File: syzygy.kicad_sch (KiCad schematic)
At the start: 5 parts, among them J3 SYZYGY_STD, U11 SN74LVC2T45YZP, U13 ADC101C021CIMK

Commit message: Incremental Progress
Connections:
- net 3V3: no longer J3.40 (+3.3V)
- net VIO: no longer J3.39 (VIO)
- net 5V renamed SYZYGY_5V
- new net SYZYGY_3V3: J3.40 (+3.3V)
- new net SYZYGY_VIO: J3.39 (VIO)
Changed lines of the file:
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@@
+	)
+	(junction
+		(at 158.75 36.83)
+		(diameter 0)
+		(color 0 0 0 0)
 	)
 	(junction
@@
 		(color 0 0 0 0)
 	)
+	(junction
+		(at 158.75 87.63)
+		(diameter 0)
+		(color 0 0 0 0)
+	)
 	(no_connect
 		(at 130.81 67.31)
@@
 	(wire
 		(pts
-			(xy 120.65 87.63) (xy 130.81 87.63)
-		)
-		(stroke
-			(width 0)
-			(type default)
-		)
-	)
-	(wire
-		(pts
 			(xy 120.65 44.45) (xy 130.81 44.45)
 		)
@@
 	(wire
 		(pts
+			(xy 158.75 87.63) (xy 158.75 92.71)
+		)
+		(stroke
+			(width 0)
+			(type default)
+		)
+	)
+	(wire
+		(pts
+			(xy 158.75 36.83) (xy 161.29 36.83)
+		)
+		(stroke
+			(width 0)
+			(type default)
+		)
+	)
+	(wire
+		(pts
 			(xy 73.66 44.45) (xy 81.28 44.45)
 		)
@@
 	(wire
 		(pts
+			(xy 128.27 87.63) (xy 130.81 87.63)
+		)
+		(stroke
+			(width 0)
+			(type default)
+		)
+	)
+	(wire
+		(pts
 			(xy 45.72 105.41) (xy 46.99 105.41)
 		)
@@
 	(wire
 		(pts
+			(xy 158.75 34.29) (xy 158.75 36.83)
+		)
+		(stroke
+			(width 0)
+			(type default)
+		)
+	)
+	(wire
+		(pts
 			(xy 158.75 41.91) (xy 168.91 41.91)
 		)
@@
 	(wire
 		(pts
+			(xy 161.29 87.63) (xy 158.75 87.63)
+		)
+		(stroke
+			(width 0)
+			(type default)
+		)
+	)
+	(wire
+		(pts
 			(xy 45.72 105.41) (xy 45.72 110.49)
 		)
@@
 	(wire
 		(pts
+			(xy 158.75 36.83) (xy 158.75 39.37)
+		)
+		(stroke
+			(width 0)
+			(type default)
+		)
+	)
+	(wire
+		(pts
 			(xy 50.8 54.61) (xy 50.8 59.69)
 		)
@@
 	(wire
 		(pts
-			(xy 158.75 87.63) (xy 168.91 87.63)
-		)
-		(stroke
-			(width 0)
-			(type default)
-		)
-	)
-	(wire
-		(pts
 			(xy 35.56 49.53) (xy 50.8 49.53)
 		)
@@
 		(pts
 			(xy 118.11 77.47) (xy 118.11 80.01)
-		)
-		(stroke
-			(width 0)
-			(type default)
-		)
-	)
-	(wire
-		(pts
-			(xy 158.75 39.37) (xy 168.91 39.37)
 		)
 		(stroke
@@
 		)
 	)
-	(label "VIO"
-		(at 120.65 87.63 0)
-		(fields_autoplaced yes)
-		(effects
-			(font
-				(size 1.27 1.27)
-			)
-			(justify left bottom)
-		)
-	)
 	(label "3V3"
 		(at 81.28 39.37 270)
@@
 		)
 	)
-	(label "3V3"
-		(at 168.91 87.63 180)
-		(fields_autoplaced yes)
-		(effects
-			(font
-				(size 1.27 1.27)
-			)
-			(justify right bottom)
-		)
-	)
 	(label "I2C_ADC.SCL"
 		(at 35.56 52.07 0)
@@
 			)
 			(justify left bottom)
+		)
+	)
+	(global_label "SYZYGY_5V"
+		(shape passive)
+		(at 161.29 36.83 0)
+		(fields_autoplaced yes)
+		(effects
+			(font
+				(size 1.27 1.27)
+			)
+			(justify left)
+		)
+		(property "Intersheetrefs" "${INTERSHEET_REFS}"
+			(at 173.3844 36.83 0)
+			(effects
+				(font
+					(size 1.27 1.27)
+				)
+				(justify left)
+				(hide yes)
+			)
+		)
+	)
+	(global_label "SYZYGY_VIO"
+		(shape passive)
+		(at 128.27 87.63 180)
+		(fields_autoplaced yes)
+		(effects
+			(font
+				(size 1.27 1.27)
+			)
+			(justify right)
+		)
+		(property "Intersheetrefs" "${INTERSHEET_REFS}"
+			(at 115.4498 87.63 0)
+			(effects
+				(font
+					(size 1.27 1.27)
+				)
+				(justify right)
+				(hide yes)
+			)
+		)
+	)
+	(global_label "SYZYGY_3V3"
+		(shape passive)
+		(at 161.29 87.63 0)
+		(fields_autoplaced yes)
+		(effects
+			(font
+				(size 1.27 1.27)
+			)
+			(justify left)
+		)
+		(property "Intersheetrefs" "${INTERSHEET_REFS}"
+			(at 174.5939 87.63 0)
+			(effects
+				(font
+					(size 1.27 1.27)
+				)
+				(justify left)
+				(hide yes)
+			)
 		)
 	)
@@
 		)
 	)
-	(hierarchical_label "5V"
-		(shape passive)
-		(at 168.91 39.37 0)
-		(fields_autoplaced yes)
-		(effects
-			(font
-				(size 1.27 1.27)
-			)
-			(justify left)
-		)
-	)
 	(hierarchical_label "TDM{FS,DATA}"
 		(shape output)
@@
 		)
 	)
-	(hierarchical_label "VIO"
-		(shape passive)
-		(at 120.65 87.63 180)
-		(fields_autoplaced yes)
-		(effects
-			(font
-				(size 1.27 1.27)
-			)
-			(justify right)
-		)
-	)
 	(hierarchical_label "I2C_C{SCL,SDA}"
 		(shape bidirectional)
@@
 			)
 			(justify left)
+		)
+	)
+	(symbol
+		(lib_id "power:PWR_FLAG")
+		(at 158.75 34.29 0)
+		(unit 1)
+		(exclude_from_sim no)
+		(in_bom yes)
+		(on_board yes)
+		(dnp no)
+		(fields_autoplaced yes)
+		(property "Reference" "#FLG03"
+			(at 158.75 32.385 0)
+			(effects
+				(font
+					(size 1.27 1.27)
+				)
+				(hide yes)
+			)
+		)
+		(property "Value" "PWR_FLAG"
+			(at 158.75 29.21 0)
+			(effects
+				(font
+					(size 1.27 1.27)
+				)
+			)
+		)
+		(property "Footprint" ""
+			(at 158.75 34.29 0)
+			(effects
+				(font
+					(size 1.27 1.27)
+				)
+				(hide yes)
+			)
+		)
+		(property "Datasheet" "~"
+			(at 158.75 34.29 0)
+			(effects
+				(font
+					(size 1.27 1.27)
+				)
+				(hide yes)
+			)
+		)
+		(property "Description" "Special symbol for telling ERC where power comes from"
+			(at 158.75 34.29 0)
+			(effects
+				(font
+					(size 1.27 1.27)
+				)
+				(hide yes)
+			)
+		)
+		(pin "1"
+		)
+		(instances
+			(project "albert"
+				(path "/b16dfd04-6bfc-4d2d-ba2c-9a843d57dfb1/c7bb0f6a-a070-4074-9132-0f05f79fd133"
+					(reference "#FLG03")
+					(unit 1)
+				)
+			)
 		)
 	)
@@
 					(unit 1)
 				)
+			)
+		)
+	)
+	(symbol
+		(lib_id "power:PWR_FLAG")
+		(at 158.75 92.71 0)
+		(mirror x)
+		(unit 1)
+		(exclude_from_sim no)
+		(in_bom yes)
+		(on_board yes)
+		(dnp no)
+		(fields_autoplaced yes)
+		(property "Reference" "#FLG04"
+			(at 158.75 94.615 0)
+			(effects
+				(font
+					(size 1.27 1.27)
+				)
+				(hide yes)
+			)
+		)
+		(property "Value" "PWR_FLAG"
+			(at 158.75 97.79 0)
+			(effects
+				(font
+					(size 1.27 1.27)
+				)
+			)
+		)
+		(property "Footprint" ""
+			(at 158.75 92.71 0)
+			(effects
+				(font
+					(size 1.27 1.27)
+				)
+				(hide yes)
+			)
+		)
+		(property "Datasheet" "~"
+			(at 158.75 92.71 0)
+			(effects
+				(font
+					(size 1.27 1.27)
+				)
+				(hide yes)
+			)
+		)
+		(property "Description" "Special symbol for telling ERC where power comes from"
+			(at 158.75 92.71 0)
+			(effects
+				(font
+					(size 1.27 1.27)
+				)
+				(hide yes)
+			)
+		)
+		(pin "1"
+		)
+		(instances
+			(project "albert"
+				(path "/b16dfd04-6bfc-4d2d-ba2c-9a843d57dfb1/c7bb0f6a-a070-4074-9132-0f05f79fd133"
+					(reference "#FLG04")
+					(unit 1)
+				)

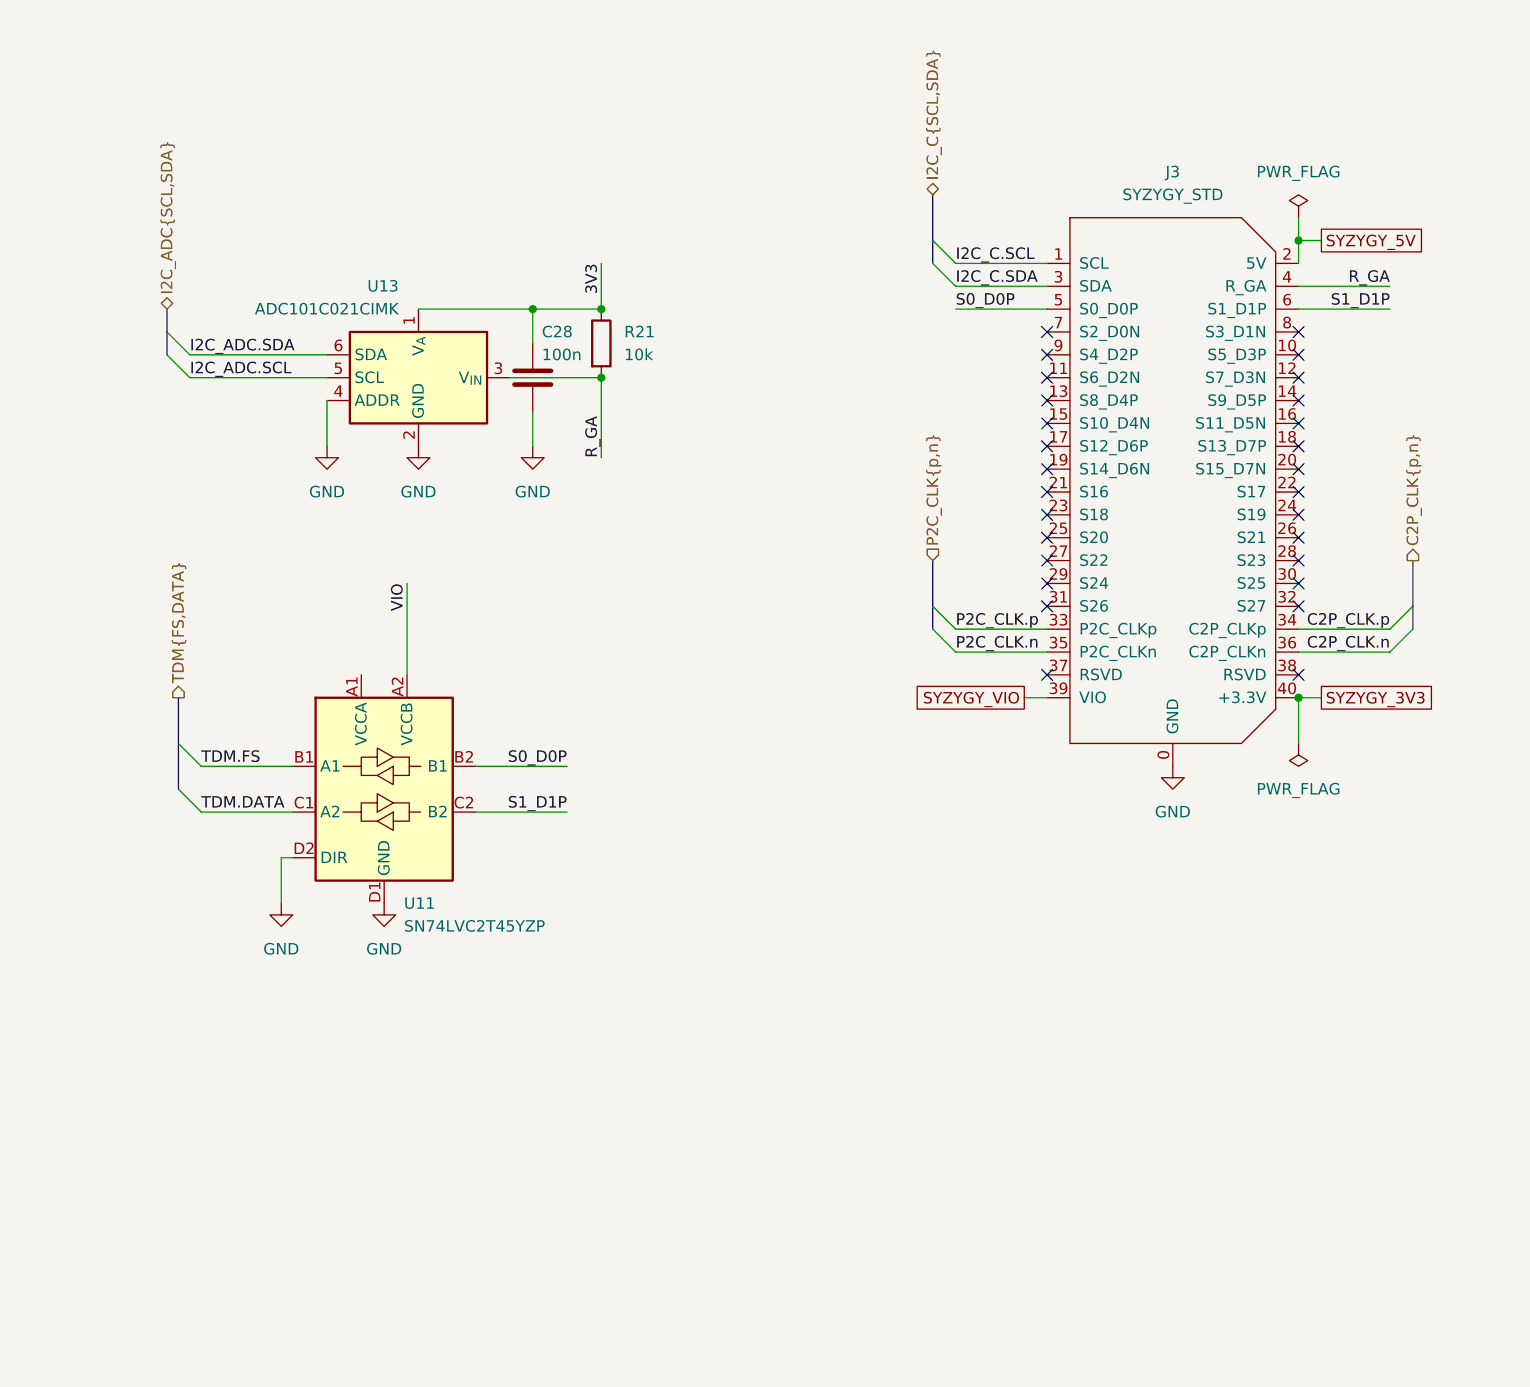
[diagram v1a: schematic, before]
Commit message: Converted connector power to global labels
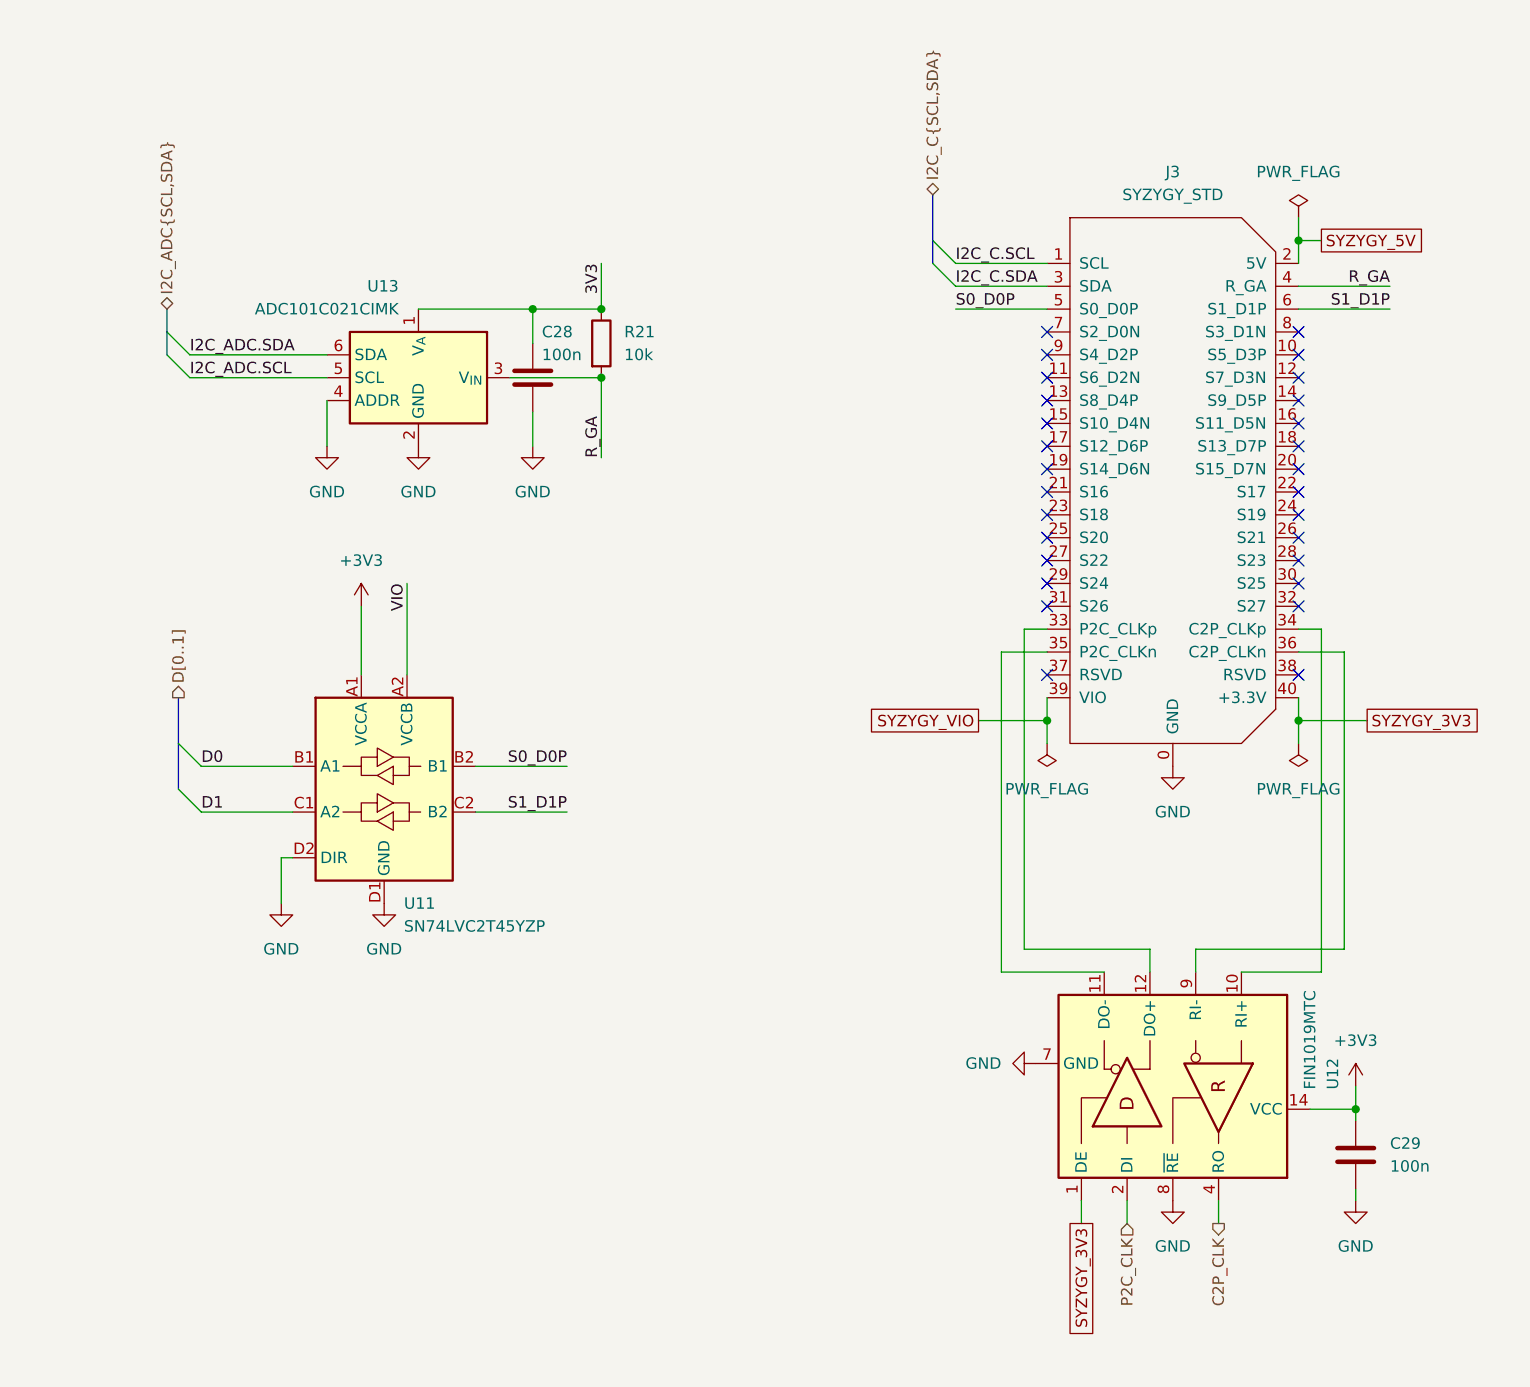
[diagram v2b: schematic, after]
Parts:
- added C29: 100n, symbol Device:C
- added U12: FIN1019MTC, Package_SO:TSSOP-14_4.4x5mm_P0.65mm, symbol Interface:FIN1019MTC
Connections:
- net GND: now also C29.2, U12.7 (GND), U12.8 (~{RE})
- net SYZYGY_3V3: now also U12.1 (DE)
- net +3V3: now reaches U11.A1 (VCCA)
- net +3V3: now also C29.1, U12.14 (VCC)
- net C2P_CLK.n: no longer names the net of J3.36 (C2P_CLKn)
- net C2P_CLK.n: now also U12.9 (RI-)
- net C2P_CLK.p: no longer names the net of J3.34 (C2P_CLKp)
- net C2P_CLK.p: now also U12.10 (RI+)
- net P2C_CLK.n: no longer names the net of J3.35 (P2C_CLKn)
- net P2C_CLK.n: now also U12.11 (DO-)
- net P2C_CLK.p: no longer names the net of J3.33 (P2C_CLKp)
- net P2C_CLK.p: now also U12.12 (DO+)
- net TDM.DATA renamed D1
- net TDM.FS renamed D0
- new net C2P_CLK: U12.4 (RO)
- new net P2C_CLK: U12.2 (DI)

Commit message: Added pMCU
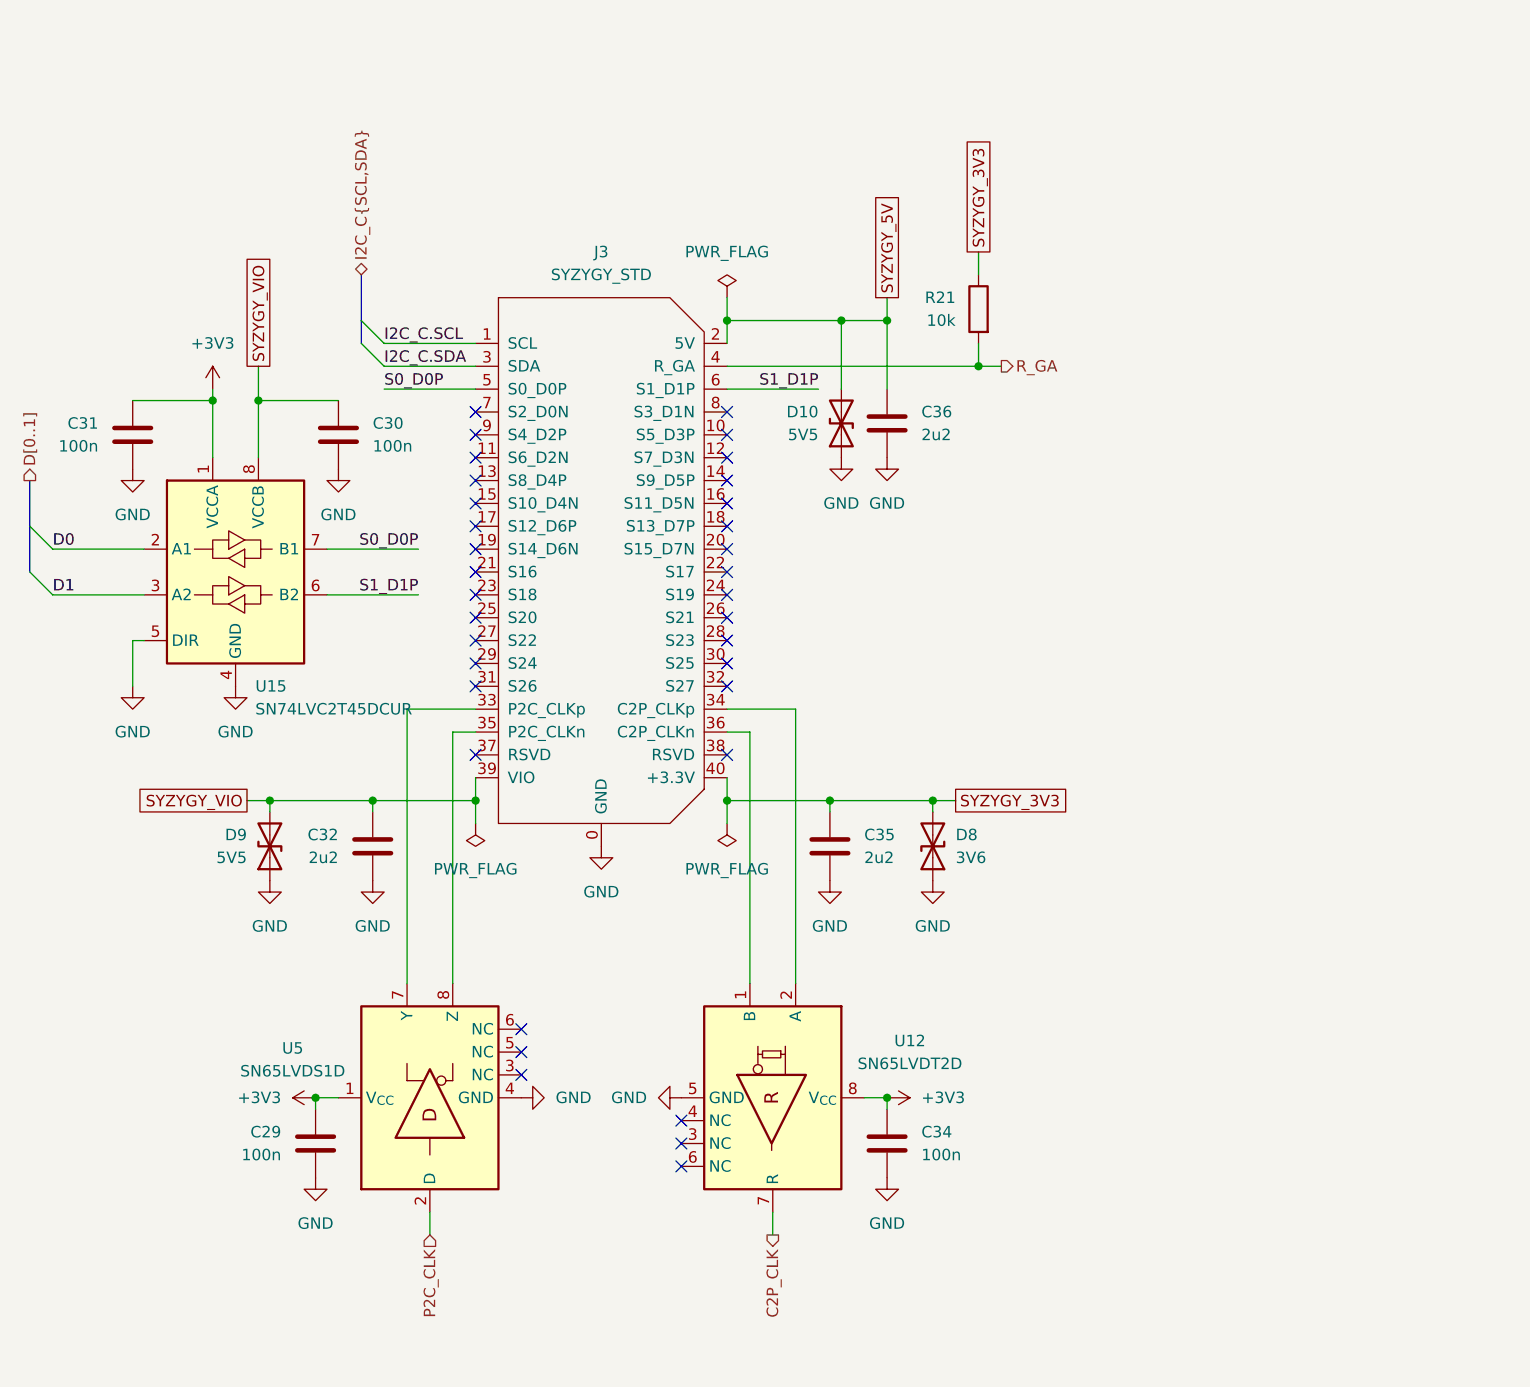
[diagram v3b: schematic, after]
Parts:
- removed C28: 100n, symbol Device:C
- removed U11: SN74LVC2T45YZP, Package_BGA:Texas_DSBGA-8_0.9x1.9mm_Layout2x4_P0.5mm, symbol Logic_LevelTranslator:SN74LVC2T45YZP
- removed U12: FIN1019MTC, Package_SO:TSSOP-14_4.4x5mm_P0.65mm, symbol Interface:FIN1019MTC
- removed U13: ADC101C021CIMK, Package_TO_SOT_SMD:SOT-23-6, symbol Analog_ADC:ADC101C021CIMK
- added C30, C31, C34: 100n, symbol Device:C
- added C32, C35, C36: 2u2, symbol Device:C
- added D10, D9: 5V5, symbol Device:D_TVS
- added D8: 3V6, symbol Device:D_TVS
- added U12: SN65LVDT2D, Package_SO:SOIC-8_3.9x4.9mm_P1.27mm, symbol Interface:SN65LVDT2D
- added U15: SN74LVC2T45DCUR, Package_SO:VSSOP-8_2.3x2mm_P0.5mm, symbol Logic_LevelTranslator:SN74LVC2T45DCUR
- added U5: SN65LVDS1D, Package_SO:SOIC-8_3.9x4.9mm_P1.27mm, symbol Interface:SN65LVDS1D
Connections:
- net 3V3 is gone; now on net SYZYGY_3V3: R21.1
- net +3V3: now also C31.1, C34.1, U12.8 (V_{CC}), U15.1 (VCCA), U5.1 (V_{CC})
- net C2P_CLK: now also U12.7 (R)
- net D0: now also U15.2 (A1)
- net D1: now also U15.3 (A2)
- net GND: now also C30.2, C31.2, C32.2, C34.2, C35.2, C36.2, D10.1 (A1), D8.1 (A1), D9.1 (A1), U12.5 (GND), U15.4 (GND), U15.5 (DIR), U5.4 (GND)
- net P2C_CLK: now also U5.2 (D)
- net S0_D0P: now also U15.7 (B1)
- net S1_D1P: now also U15.6 (B2)
- net SYZYGY_3V3: now also C35.1, D8.2 (A2)
- net SYZYGY_5V: now also C36.1, D10.2 (A2)
- net SYZYGY_VIO: now also C30.1, C32.1, D9.2 (A2), U15.8 (VCCB)
- net at J3.34 (C2P_CLKp): now also U12.2 (A)
- net at J3.35 (P2C_CLKn): now also U5.8 (Z)
- net at J3.33 (P2C_CLKp): now also U5.7 (Y)
- net at J3.36 (C2P_CLKn): now also U12.1 (B)
- no-connect marks 28 -> 34
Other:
- moved on the sheet: J3
